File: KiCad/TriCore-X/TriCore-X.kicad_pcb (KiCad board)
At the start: 2 copper layers, 15 parts, among them U1 RK3568B2, U2 XC7A35T-FGG484, U3 TPS56637RPAR

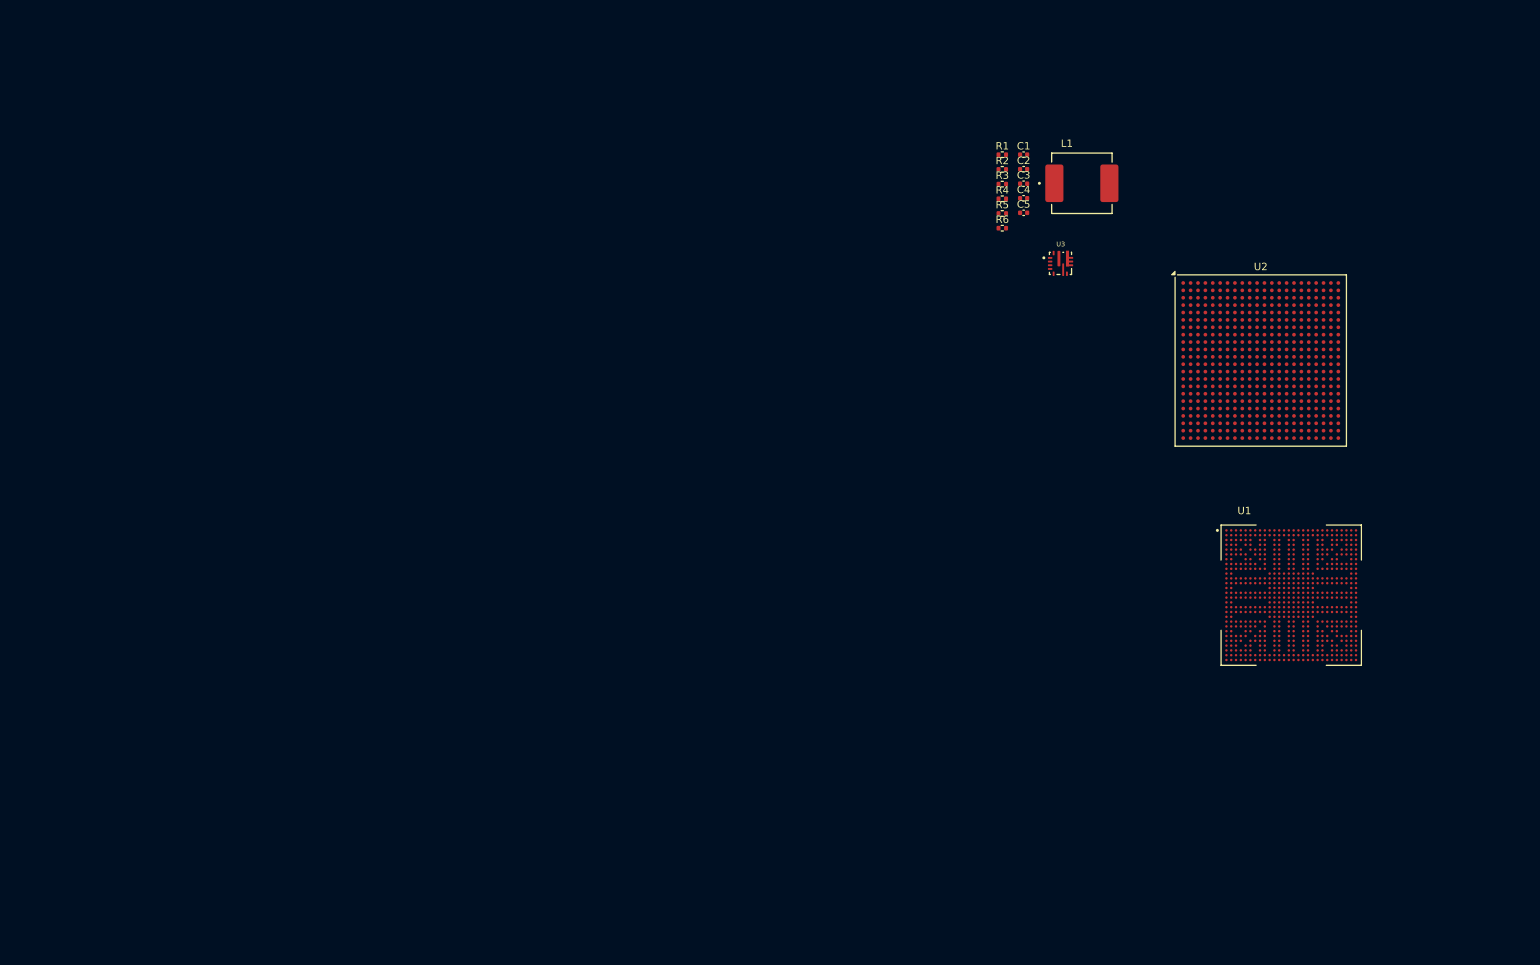
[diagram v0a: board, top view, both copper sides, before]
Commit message: feat: design 5V and 12V power rails (schematic & PCB)
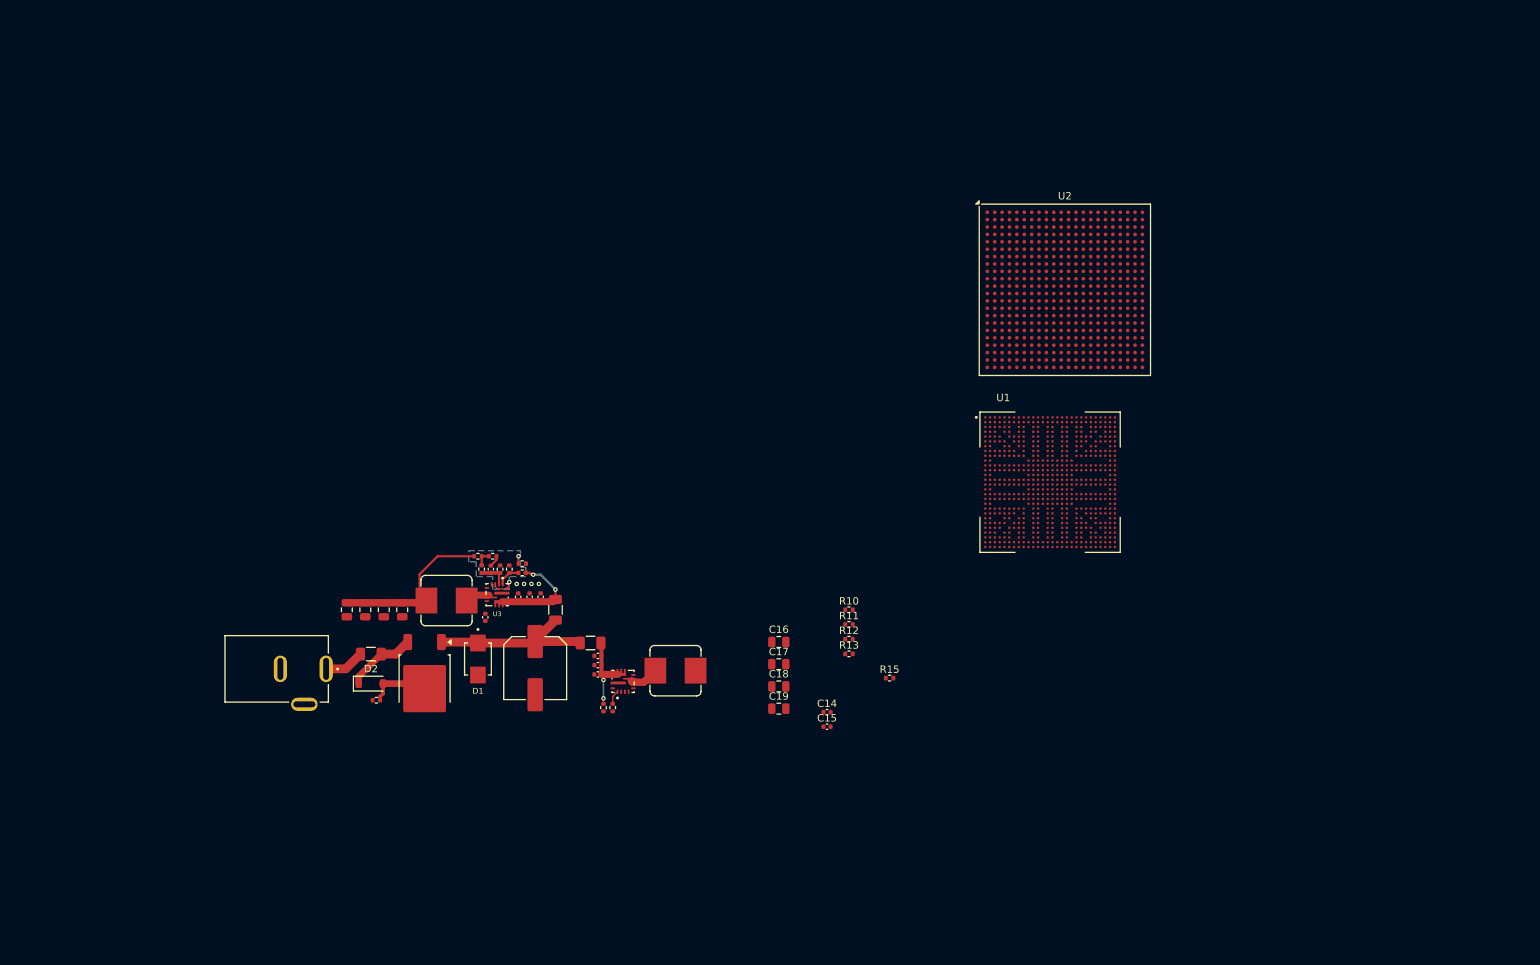
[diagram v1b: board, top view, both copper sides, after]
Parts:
- added C10: 220uF, Capacitor_SMD:C_Elec_8x10.2, F.Cu at (118.5, 107.7)
- added C11: 10uF, Capacitor_SMD:C_0402_1005Metric, F.Cu at (127.0, 106.0)
- added C12: 10uF, Capacitor_SMD:C_0402_1005Metric, F.Cu at (127.0, 107.2)
- added C13: 0.1uF, Capacitor_SMD:C_0402_1005Metric, F.Cu at (127.0, 108.5)
- added C14: 0.1uF, Capacitor_SMD:C_0402_1005Metric, F.Cu at (158.0, 113.6)
- added C15: 100pF, Capacitor_SMD:C_0402_1005Metric, F.Cu at (158.0, 115.6)
- added C16: 22uF, Capacitor_SMD:C_0805_2012Metric, F.Cu at (151.5, 104.1)
- added C17: 22uF, Capacitor_SMD:C_0805_2012Metric, F.Cu at (151.5, 107.1)
- added C18: 22uF, Capacitor_SMD:C_0805_2012Metric, F.Cu at (151.5, 110.1)
- added C19: 22uF, Capacitor_SMD:C_0805_2012Metric, F.Cu at (151.5, 113.1)
- added C6: 22uF, Capacitor_SMD:C_0805_2012Metric, F.Cu at (100.5, 99.8)
- added C7: 22uF, Capacitor_SMD:C_0805_2012Metric, F.Cu at (98.0, 99.8)
- added C8: 22uF, Capacitor_SMD:C_0805_2012Metric, F.Cu at (95.5, 99.8)
- added C9: 22uF, Capacitor_SMD:C_0805_2012Metric, F.Cu at (93.0, 99.8)
- added D1: SMBJ26A, SMBJ26A:DIOM4336X265N, F.Cu at (110.8, 106.4)
- added D2: Zener_15V, Diode_SMD:D_SOD-123, F.Cu at (96.2, 109.8)
- added F1: 3A Fuse, Fuse:Fuse_1206_3216Metric, F.Cu at (121.2, 99.8)
- added F2: 3A Fuse, Fuse:Fuse_1206_3216Metric, F.Cu at (126.0, 104.2)
- added F3: 7A Fuse, Fuse:Fuse_1206_3216Metric, F.Cu at (96.2, 105.8)
- added J1: PJ-035DH, DC_INPUT:CUI_PJ-035DH, F.Cu at (90.2, 107.8)
- added L2: 5.6uH, Inductor_SMD:L_Bourns_SRP7028A_7.3x6.6mm, F.Cu at (137.5, 108.0)
- added Q1: AOD407, Package_TO_SOT_SMD:TO-252-2, F.Cu at (103.5, 109.2)
- added R10: 20K, Resistor_SMD:R_0402_1005Metric, F.Cu at (161.0, 99.8)
- added R11: 49.9R, Resistor_SMD:R_0402_1005Metric, F.Cu at (161.0, 101.7)
- added R12: 191K, Resistor_SMD:R_0402_1005Metric, F.Cu at (161.0, 103.7)
- added R13: 10K, Resistor_SMD:R_0402_1005Metric, F.Cu at (161.0, 105.7)
- added R14: 0R, Resistor_SMD:R_0402_1005Metric, F.Cu at (116.8, 93.5)
- added R15: 0R, Resistor_SMD:R_0402_1005Metric, F.Cu at (166.5, 109.0)
- added R7: 10K, Resistor_SMD:R_0402_1005Metric, F.Cu at (97.0, 112.0)
- added R8: 169k, Resistor_SMD:R_0402_1005Metric, F.Cu at (127.8, 113.0)
- added R9: 36.1k, Resistor_SMD:R_0402_1005Metric, F.Cu at (129.0, 113.0)
- added U4: TPS56637RPAR, TPS56637RPAR:CONV_TPS56637RPAR, F.Cu at (130.4, 109.5)
- L1: value IHLP3232DZER3R3M11 -> 3.3uH; footprint IHLP3232DZER3R3M11:INDM8681X400N -> Inductor_SMD:L_Bourns_SRP7028A_7.3x6.6mm
- R2: value 36.1R -> 36.1k
- moved L1 102.9 mm to (106.5, 98.5), turned to 180 degrees
- moved C4 92.4 mm to (111.8, 100.8), turned to 90 degrees
- moved C1 88.7 mm to (119.2, 98.0), turned to 90 degrees
- moved U3 88.5 mm to (113.3, 97.7), turned to -90 degrees
- moved C2 88.5 mm to (117.8, 98.0), turned to 90 degrees
- moved C3 88.4 mm to (116.2, 98.0), turned to 90 degrees
- moved R3 87.1 mm to (110.8, 92.5)
- moved C5 86.8 mm to (112.5, 94.2), turned to -90 degrees
- moved R4 86.5 mm to (111.2, 94.2), turned to -90 degrees
- moved R1 86.2 mm to (116.8, 94.8), turned to 180 degrees
- moved R2 85.9 mm to (115.0, 94.2), turned to 90 degrees
- moved R5 83.3 mm to (113.8, 94.3), turned to 90 degrees
- moved R6 82.1 mm to (112.8, 92.5), turned to 180 degrees
- moved U1 36.1 mm to (188.2, 82.5)
- moved U2 28.2 mm to (190.2, 56.4)
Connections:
- net Net-(L1-Pad2) renamed /power/5V_Rail
- C5 pad 2: Net-(C5-Pad2) -> Net-(U3-FB)
- R4 pad 2: Net-(C5-Pad2) -> Net-(U3-FB)
- R5 pad 1: Net-(C5-Pad2) -> Net-(U3-FB)
- R5 pad 2: unconnected-(R5-Pad2) -> GNDA
- U3 pad 2: unconnected-(U3-FB-Pad2) -> Net-(U3-FB)
- U3 pad 3: unconnected-(U3-AGND-Pad3) -> GNDA
- U3 pad 4: unconnected-(U3-PG-Pad4) -> /power/5V_OK
- U3 pad 9: unconnected-(U3-PGND-Pad9) -> GND
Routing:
- net /power/5V_Rail: track 0.00 -> 23.2 mm
- net /power/Power_Input: track 0.00 -> 23.1 mm
- net Net-(U3-VIN): track 0.00 -> 14.1 mm, vias 0 -> 2
- net Net-(U4-VIN): track 0.00 -> 10.7 mm, vias 0 -> 2
- net Net-(D2-K): track 0.00 -> 9.53 mm
- net Net-(D2-A): track 0.00 -> 8.44 mm
- net Net-(F3-Pad1): track 0.00 -> 5.48 mm
- net Net-(U3-SW): track 0.00 -> 5.03 mm
- net Net-(U3-FB): track 0.00 -> 4.12 mm
- net GNDA: track 0.00 -> 4.03 mm, vias 0 -> 2
- net Net-(U4-SW): track 0.00 -> 4.00 mm
- net Net-(U3-EN): track 0.00 -> 2.92 mm
- net Net-(R3-Pad2): track 0.00 -> 2.22 mm
- net Net-(U4-EN): track 0.00 -> 1.91 mm
- net Net-(C5-Pad1): track 0.00 -> 1.58 mm
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- added copper zone on B.Cu, net GNDA
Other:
- copper layers 2 -> 6
- board text added: "${REFERENCE}"

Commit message: feat : add some Expansion Ports (work in progress)
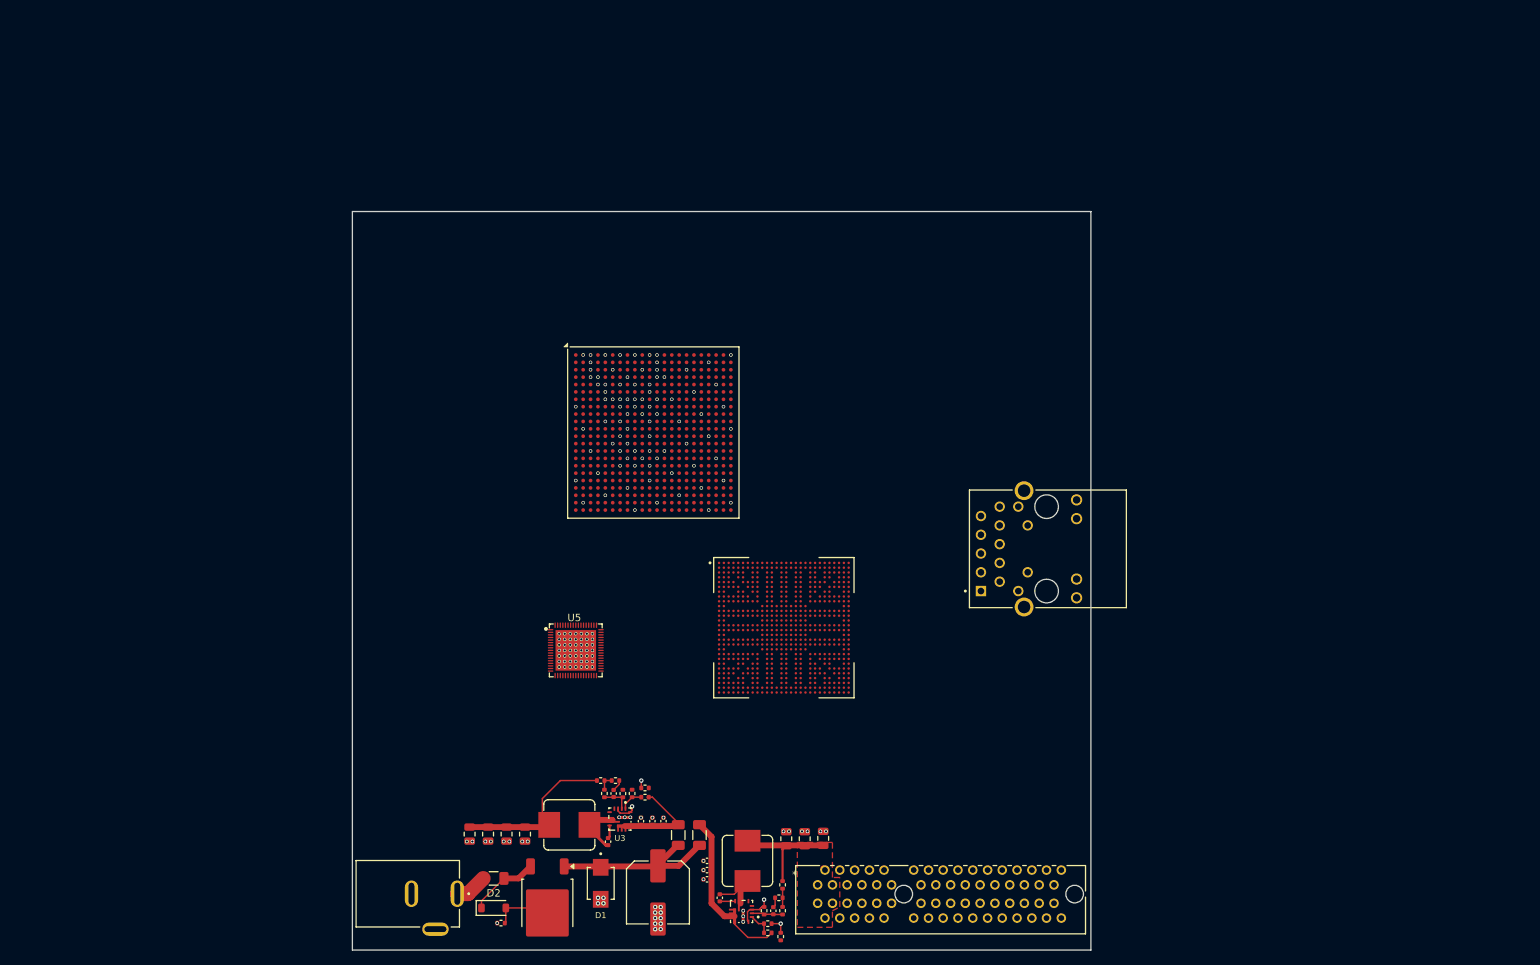
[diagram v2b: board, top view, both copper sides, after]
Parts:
- removed C16: 22uF, Capacitor_SMD:C_0805_2012Metric
- added J2: 877159106, 877159106:CONN_87715-9106_MOL, F.Cu at (156.8, 137.0)
- added J3: LPJG0926HENL, LPJG0926HENL:LINK-PP_LPJG0926HENL, F.Cu at (187.8, 91.5)
- added U5: RK809-5, RK809-5:QFN-68_L7.0-W7.0-P0.35-BL-EP5.5, F.Cu at (123.8, 105.2)
- moved U2 59.0 mm to (134.5, 75.8)
- moved U1 41.1 mm to (152.2, 102.2)
- moved R10 40.1 mm to (151.5, 138.8)
- moved R15 38.0 mm to (151.8, 144.0), turned to -90 degrees
- moved R12 37.9 mm to (152.0, 140.5), turned to -90 degrees
- moved R8 37.8 mm to (150.0, 143.5), turned to 180 degrees
- moved R13 36.6 mm to (149.5, 140.5), turned to 90 degrees
- moved R11 36.4 mm to (152.0, 137.0), turned to -90 degrees
- moved R9 36.0 mm to (150.0, 142.2), turned to 0 degrees
- moved J1 35.2 mm to (108.0, 138.2)
- moved U4 35.0 mm to (146.4, 140.6), turned to 180 degrees
- moved F1 34.7 mm to (137.9, 130.2)
- moved C4 34.6 mm to (128.4, 131.1)
- moved U3 34.6 mm to (130.0, 128.1)
- moved C1 34.6 mm to (135.9, 128.4)
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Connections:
- net /power/12V_OK renamed 12V_OK
- net /power/5V_OK renamed 5V_OK
- net /power/5V_Rail renamed +5V
- net /power/PCIE_12V_Rail renamed +12V
- R7 pad 1: unconnected-(R7-Pad1) -> Net-(D2-A)
- R7 pad 2: unconnected-(R7-Pad2) -> GND
- U1 pad A12: unconnected-(U1E-DDR_DQ4_B-PadA12) -> /DDR4/DDR_DQ4_B
- U1 pad A13: unconnected-(U1E-DDR_DQ13_B-PadA13) -> /DDR4/DDR_DQ13_B
- U1 pad A16: unconnected-(U1E-DDR_DQ8_B-PadA16) -> /DDR4/DDR_DQ8_B
- U1 pad A17: unconnected-(U1E-DDR_DQ10_B-PadA17) -> /DDR4/DDR_DQ10_B
- U1 pad A9: unconnected-(U1E-DDR_DQ1_B-PadA9) -> /DDR4/DDR_DQ1_B
- U1 pad B10: unconnected-(U1E-DDR_DQ0_B-PadB10) -> /DDR4/DDR_DQ0_B
- U1 pad B13: unconnected-(U1E-DDR_DQ12_B-PadB13) -> /DDR4/DDR_DQ12_B
- U1 pad B14: unconnected-(U1E-DDR_DQ15_B-PadB14) -> /DDR4/DDR_DQ15_B
- U1 pad B17: unconnected-(U1E-DDR_DQ9_B-PadB17) -> /DDR4/DDR_DQ9_B
- U1 pad B18: unconnected-(U1E-DDR_DQ11_B-PadB18) -> /DDR4/DDR_DQ11_B
- U1 pad D1: unconnected-(U1E-DDR_DQ3_A-PadD1) -> /DDR4/DDR_DQ3_A
- U1 pad D12: unconnected-(U1E-DDR_DQ2_B-PadD12) -> /DDR4/DDR_DQ2_B
- U1 pad D15: unconnected-(U1E-DDR_DQ5_B-PadD15) -> /DDR4/DDR_DQ5_B
- U1 pad D17: unconnected-(U1E-DDR_DQ14_B-PadD17) -> /DDR4/DDR_DQ14_B
- U1 pad E1: unconnected-(U1E-DDR_DQ1_A-PadE1) -> /DDR4/DDR_DQ1_A
- U1 pad E12: unconnected-(U1E-DDR_DQ3_B-PadE12) -> /DDR4/DDR_DQ3_B
- U1 pad E14: unconnected-(U1E-DDR_DQ7_B-PadE14) -> /DDR4/DDR_DQ7_B
- U1 pad E15: unconnected-(U1E-DDR_DQ6_B-PadE15) -> /DDR4/DDR_DQ6_B
- U1 pad E2: unconnected-(U1E-DDR_DQ2_A-PadE2) -> /DDR4/DDR_DQ2_A
- U1 pad F2: unconnected-(U1E-DDR_DQ0_A-PadF2) -> /DDR4/DDR_DQ0_A
- U1 pad H1: unconnected-(U1E-DDR_DQ6_A-PadH1) -> /DDR4/DDR_DQ6_A
- U1 pad H4: unconnected-(U1E-DDR_DQ7_A-PadH4) -> /DDR4/DDR_DQ7_A
- U1 pad J1: unconnected-(U1E-DDR_DQ4_A-PadJ1) -> /DDR4/DDR_DQ4_A
- U1 pad J2: unconnected-(U1E-DDR_DQ5_A-PadJ2) -> /DDR4/DDR_DQ5_A
- U1 pad J6: unconnected-(U1E-DDR_DQ13_A-PadJ6) -> /DDR4/DDR_DQ13_A
- U1 pad J7: unconnected-(U1E-DDR_DQ14_A-PadJ7) -> /DDR4/DDR_DQ14_A
- U1 pad K2: unconnected-(U1E-DDR_DQ12_A-PadK2) -> /DDR4/DDR_DQ12_A
- U1 pad L4: unconnected-(U1E-DDR_DQ15_A-PadL4) -> /DDR4/DDR_DQ15_A
- U1 pad L6: unconnected-(U1E-DDR_DQ11_A-PadL6) -> /DDR4/DDR_DQ11_A
- U1 pad L7: unconnected-(U1E-DDR_DQ10_A-PadL7) -> /DDR4/DDR_DQ10_A
- U1 pad M1: unconnected-(U1E-DDR_DQ8_A-PadM1) -> /DDR4/DDR_DQ8_A
- U1 pad N2: unconnected-(U1E-DDR_DQ9_A-PadN2) -> /DDR4/DDR_DQ9_A
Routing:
- net +12V: track 0.00 -> 16.7 mm
- net Net-(U4-VIN): track 10.7 -> 22.7 mm, vias 2 -> 0
- net GNDA: track 4.03 -> 11.5 mm, vias 2 -> 4
- net Net-(U3-SW): track 5.03 -> 10.1 mm
- net Net-(U4-SW): track 4.00 -> 9.02 mm
- net Net-(U4-FB): track 0.00 -> 4.24 mm
- net Net-(R10-Pad2): track 0.00 -> 2.48 mm
- net Net-(U4-BOOT): track 0.00 -> 2.09 mm
- net Net-(U3-BOOT): track 0.00 -> 1.79 mm
- net Net-(C15-Pad1): track 0.00 -> 1.37 mm
- net Net-(U4-EN): track 1.91 -> 3.26 mm
- net Net-(U3-VIN): track 14.1 -> 12.7 mm, vias 2 -> 0
- net Net-(F3-Pad1): track 5.48 -> 4.38 mm
- net /power/Power_Input: track 23.1 -> 23.6 mm
- net GND: vias 4 -> 177
- added copper zone on F.Cu, net +12V
- added copper zone on In1.Cu, net GND
- added copper zone on In4.Cu, net GND
- added copper zone on In1.Cu, net GNDA
- removed copper zone on B.Cu, net GNDA
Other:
- board outline added: 100 x 100 mm
- board text removed: "${REFERENCE}"

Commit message: feat : add ESP32-S3-WROOM-1 (work in progress)
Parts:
- removed C19: 22uF, Capacitor_SMD:C_0805_2012Metric
- added C16: 22uF, Capacitor_SMD:C_0805_2012Metric, F.Cu at (152.5, 130.8)
- added J4: 1054500101, TYPE-C:MOLEX_1054500101, F.Cu at (193.5, 87.2)
- added J5: USB-A-D-X-X-TH-R, TYPE-A:SAMTEC_USB-A-D-X-X-TH-R, F.Cu at (180.0, 69.8)
- added U6: ESP32-S3-WROOM-1, RF_Module:ESP32-S3-WROOM-1, F.Cu at (161.8, 59.0)
- U2: value XC7A35T-FGG484 -> XC7A100T-FGG484
- moved J3 15.1 mm to (182.8, 105.8)
- moved U2 12.8 mm to (122.5, 71.2)
- moved U1 8.88 mm to (143.5, 104.0)
- moved C17 2.50 mm to (155.0, 130.8)
- moved C18 2.50 mm to (157.5, 130.8)
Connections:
- U2 pad AA10: (no net) -> unconnected-(U2A-IO_L9P_T1_DQS_13-PadAA10)
- U2 pad AA11: (no net) -> unconnected-(U2A-IO_L9N_T1_DQS_13-PadAA11)
- U2 pad AA13: (no net) -> unconnected-(U2A-IO_L3P_T0_DQS_13-PadAA13)
- U2 pad AA14: (no net) -> unconnected-(U2A-IO_L5N_T0_13-PadAA14)
- U2 pad AA15: (no net) -> unconnected-(U2A-IO_L4P_T0_13-PadAA15)
- U2 pad AA16: (no net) -> unconnected-(U2A-IO_L1N_T0_13-PadAA16)
- U2 pad AA9: (no net) -> unconnected-(U2A-IO_L8P_T1_13-PadAA9)
- U2 pad AB10: (no net) -> unconnected-(U2A-IO_L8N_T1_13-PadAB10)
- U2 pad AB11: (no net) -> unconnected-(U2A-IO_L7P_T1_13-PadAB11)
- U2 pad AB12: (no net) -> unconnected-(U2A-IO_L7N_T1_13-PadAB12)
- U2 pad AB13: (no net) -> unconnected-(U2A-IO_L3N_T0_DQS_13-PadAB13)
- U2 pad AB15: (no net) -> unconnected-(U2A-IO_L4N_T0_13-PadAB15)
- U2 pad AB16: (no net) -> unconnected-(U2A-IO_L2P_T0_13-PadAB16)
- U2 pad AB17: (no net) -> unconnected-(U2A-IO_L2N_T0_13-PadAB17)
- U2 pad T14: (no net) -> unconnected-(U2A-IO_L15P_T2_DQS_13-PadT14)
- U2 pad T15: (no net) -> unconnected-(U2A-IO_L15N_T2_DQS_13-PadT15)
- U2 pad T16: (no net) -> unconnected-(U2A-IO_L17P_T2_13-PadT16)
- U2 pad U15: (no net) -> unconnected-(U2A-IO_L14P_T2_SRCC_13-PadU15)
- U2 pad U16: (no net) -> unconnected-(U2A-IO_L17N_T2_13-PadU16)
- U2 pad V10: (no net) -> unconnected-(U2A-IO_L10P_T1_13-PadV10)
- U2 pad V13: (no net) -> unconnected-(U2A-IO_L13P_T2_MRCC_13-PadV13)
- U2 pad V14: (no net) -> unconnected-(U2A-IO_L13N_T2_MRCC_13-PadV14)
- U2 pad V15: (no net) -> unconnected-(U2A-IO_L14N_T2_SRCC_13-PadV15)
- U2 pad W10: (no net) -> unconnected-(U2A-IO_L10N_T1_13-PadW10)
- U2 pad W11: (no net) -> unconnected-(U2A-IO_L12P_T1_MRCC_13-PadW11)
- U2 pad W12: (no net) -> unconnected-(U2A-IO_L12N_T1_MRCC_13-PadW12)
- U2 pad W14: (no net) -> unconnected-(U2A-IO_L6P_T0_13-PadW14)
- U2 pad W15: (no net) -> unconnected-(U2A-IO_L16P_T2_13-PadW15)
- U2 pad W16: (no net) -> unconnected-(U2A-IO_L16N_T2_13-PadW16)
- U2 pad Y11: (no net) -> unconnected-(U2A-IO_L11P_T1_SRCC_13-PadY11)
- U2 pad Y12: (no net) -> unconnected-(U2A-IO_L11N_T1_SRCC_13-PadY12)
- U2 pad Y13: (no net) -> unconnected-(U2A-IO_L5P_T0_13-PadY13)
- U2 pad Y14: (no net) -> unconnected-(U2A-IO_L6N_T0_VREF_13-PadY14)
- U2 pad Y16: (no net) -> unconnected-(U2A-IO_L1P_T0_13-PadY16)
- U2 pad Y17: (no net) -> unconnected-(U2A-IO_0_13-PadY17)
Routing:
- net GND: vias 177 -> 90
